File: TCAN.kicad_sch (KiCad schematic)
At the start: 5 parts

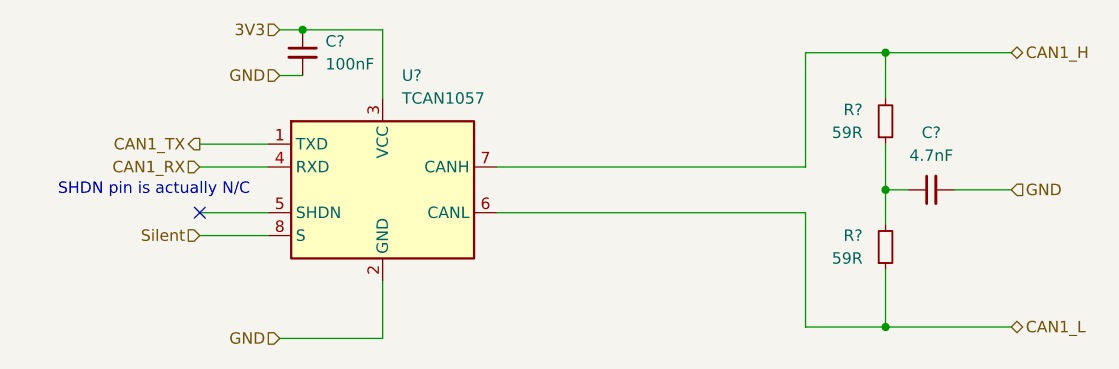
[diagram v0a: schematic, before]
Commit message: Finish routing and add option for using batt mon pads as I2C lines for added GPS
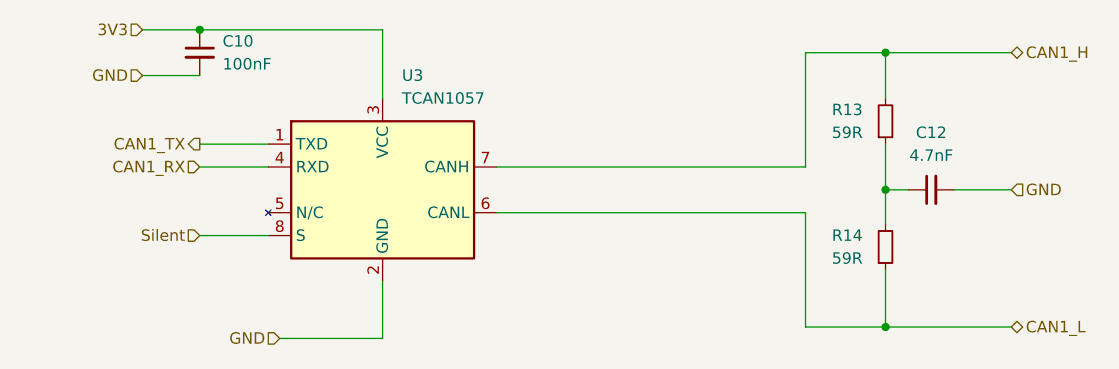
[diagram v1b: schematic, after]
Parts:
- U3: renamed from U?; symbol Interface_CAN_LIN:TCAN330G -> Mad_Symbols:TCAN1057
- gave numbers to parts that had none: 4
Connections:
- net GND: now also U3.9 (GND)
- no-connect marks 1 -> 0
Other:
- note removed: "SHDN pin is actually N/C"
- moved on the sheet: C10
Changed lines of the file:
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@@
 	(generator_version "9.0")
 	(paper "A4")
-	(text "SHDN pin is actually N/C"
-		(exclude_from_sim no)
-		(at 124.46 88.9 0)
-		(effects
-			(font
-				(size 1.27 1.27)
-			)
-		)
-	)
 	(junction
-		(at 140.97 71.12)
+		(at 129.54 71.12)
 		(diameter 0)
 		(color 0 0 0 0)
@@
 		(color 0 0 0 0)
 	)
-	(no_connect
-		(at 129.54 91.44)
-	)
 	(wire
 		(pts
@@
 	(wire
 		(pts
-			(xy 138.43 71.12) (xy 140.97 71.12)
-		)
-		(stroke
-			(width 0)
-			(type default)
-		)
-	)
-	(wire
-		(pts
-			(xy 138.43 76.2) (xy 140.97 76.2)
+			(xy 123.19 71.12) (xy 129.54 71.12)
+		)
+		(stroke
+			(width 0)
+			(type default)
+		)
+	)
+	(wire
+		(pts
+			(xy 123.19 76.2) (xy 129.54 76.2)
 		)
 		(stroke
@@
 	(wire
 		(pts
-			(xy 140.97 71.12) (xy 149.86 71.12)
-		)
-		(stroke
-			(width 0)
-			(type default)
-		)
-	)
-	(wire
-		(pts
 			(xy 129.54 83.82) (xy 137.16 83.82)
 		)
@@
 	(wire
 		(pts
-			(xy 129.54 91.44) (xy 137.16 91.44)
-		)
-		(stroke
-			(width 0)
-			(type default)
-		)
-	)
-	(wire
-		(pts
 			(xy 205.74 73.66) (xy 205.74 78.74)
 		)
@@
 		(pts
 			(xy 196.85 104.14) (xy 196.85 91.44)
+		)
+		(stroke
+			(width 0)
+			(type default)
+		)
+	)
+	(wire
+		(pts
+			(xy 129.54 71.12) (xy 149.86 71.12)
 		)
 		(stroke
@@
 	(hierarchical_label "3V3"
 		(shape input)
-		(at 138.43 71.12 180)
+		(at 123.19 71.12 180)
 		(effects
 			(font
@@
 	(hierarchical_label "GND"
 		(shape input)
-		(at 138.43 76.2 180)
+		(at 123.19 76.2 180)
 		(effects
 			(font
@@
 		(dnp no)
 		(fields_autoplaced yes)
-		(property "Reference" "C?"
+		(property "Reference" "C12"
 			(at 210.8263 82.55 90)
 			(effects
@@
 			(project "L431_RC_Periph"
 				(path "/4cee0169-48cd-4af2-8890-7045155e0b79/6992b08b-1fa8-468e-a7a3-ba5f0cdd154c/59667026-08f2-47e2-8be4-f096db63e523"
-					(reference "C?")
+					(reference "C12")
 					(unit 1)
 				)
@@
 	)
 	(symbol
-		(lib_id "Interface_CAN_LIN:TCAN330G")
+		(lib_id "Mad_Symbols:TCAN1057")
 		(at 149.86 88.9 0)
 		(unit 1)
@@
 		(dnp no)
 		(fields_autoplaced yes)
-		(property "Reference" "U?"
+		(property "Reference" "U3"
 			(at 152.0033 76.2 0)
 			(effects
@@
 		)
 		(pin "7"
+		)
+		(pin "9"
 		)
 		(instances
 			(project "L431_RC_Periph"
 				(path "/4cee0169-48cd-4af2-8890-7045155e0b79/6992b08b-1fa8-468e-a7a3-ba5f0cdd154c/59667026-08f2-47e2-8be4-f096db63e523"
-					(reference "U?")
+					(reference "U3")
 					(unit 1)
 				)
@@
 	(symbol
 		(lib_id "Device:C_Small")
-		(at 140.97 73.66 0)
+		(at 129.54 73.66 0)
 		(mirror y)
 		(unit 1)
@@
 		(dnp no)
 		(fields_autoplaced yes)
-		(property "Reference" "C?"
-			(at 143.51 72.3962 0)
+		(property "Reference" "C10"
+			(at 132.08 72.3962 0)
 			(effects
 				(font
@@
 		)
 		(property "Value" "100nF"
-			(at 143.51 74.9362 0)
+			(at 132.08 74.9362 0)
 			(effects
 				(font
@@
 		)
 		(property "Footprint" "Capacitor_SMD:C_0402_1005Metric"
-			(at 140.97 73.66 0)
+			(at 129.54 73.66 0)
 			(effects
 				(font
@@
 		)
 		(property "Datasheet" "https://www.yageo.com/upload/media/product/productsearch/datasheet/mlcc/UPY-GPHC_X7R_6.3V-to-250V_24.pdf"
-			(at 140.97 73.66 0)
+			(at 129.54 73.66 0)
 			(effects
 				(font
@@
 		)
 		(property "Description" "0.1 µF ±10% 25V Ceramic Capacitor X7R 0402 (1005 Metric)"
-			(at 140.97 73.66 0)
+			(at 129.54 73.66 0)
 			(effects
 				(font
@@
 		)
 		(property "Price" "$0.17"
-			(at 140.97 73.66 0)
+			(at 129.54 73.66 0)
 			(effects
 				(font
@@
 		)
 		(property "Interface" ""
-			(at 140.97 73.66 0)
+			(at 129.54 73.66 0)
 			(effects
 				(font
@@
 		)
 		(property "Rating" "CAP 0402 50V 100 NF X7R"
-			(at 140.97 73.66 0)
+			(at 129.54 73.66 0)
 			(effects
 				(font
@@
 		)
 		(property "Supplier" "Digikey"
-			(at 140.97 73.66 0)
+			(at 129.54 73.66 0)
 			(effects
 				(font
@@
 		)
 		(property "Supplier PN" "13-CC0402KPX7R9BB104CT-ND"
-			(at 140.97 73.66 0)
+			(at 129.54 73.66 0)
 			(effects
 				(font
@@
 		)
 		(property "Manufacturer" "YAGEO"
-			(at 140.97 73.66 0)
+			(at 129.54 73.66 0)
 			(effects
 				(font
@@
 		)
 		(property "MPN" "CC0402KPX7R9BB104"
-			(at 140.97 73.66 0)
+			(at 129.54 73.66 0)
 			(effects
 				(font
@@
 		)
 		(property "Substitute" ""
-			(at 140.97 73.66 0)
+			(at 129.54 73.66 0)
 			(effects
 				(font
@@
 		)
 		(property "LCSC" "C432917"
-			(at 140.97 73.66 0)
+			(at 129.54 73.66 0)
 			(effects
 				(font
@@
 			(project "L431_RC_Periph"
 				(path "/4cee0169-48cd-4af2-8890-7045155e0b79/6992b08b-1fa8-468e-a7a3-ba5f0cdd154c/59667026-08f2-47e2-8be4-f096db63e523"
-					(reference "C?")
+					(reference "C10")
 					(unit 1)
 				)
@@
 		(on_board yes)
 		(dnp no)
-		(property "Reference" "R?"
+		(property "Reference" "R13"
 			(at 203.2 80.0099 0)
 			(effects
@@
 			)
 		)
-		(property "Description" "59 Ohms ±1% 0.063W, 1/16W Chip Resistor 0402 (1005 Metric) Moisture Resistant Thick Film"
+		(property "Description" "Resistor, small symbol"
 			(at 205.74 81.28 0)
 			(effects
@@
 			(project "L431_RC_Periph"
 				(path "/4cee0169-48cd-4af2-8890-7045155e0b79/6992b08b-1fa8-468e-a7a3-ba5f0cdd154c/59667026-08f2-47e2-8be4-f096db63e523"
-					(reference "R?")
+					(reference "R13")
 					(unit 1)
 				)
@@
 		(on_board yes)
 		(dnp no)
-		(property "Reference" "R?"
+		(property "Reference" "R14"
 			(at 203.2 93.9799 0)
 			(effects
@@
 			)
 		)
-		(property "Description" "59 Ohms ±1% 0.063W, 1/16W Chip Resistor 0402 (1005 Metric) Moisture Resistant Thick Film"
+		(property "Description" "Resistor, small symbol"
 			(at 205.74 95.25 0)
 			(effects
@@
 			(project "L431_RC_Periph"
 				(path "/4cee0169-48cd-4af2-8890-7045155e0b79/6992b08b-1fa8-468e-a7a3-ba5f0cdd154c/59667026-08f2-47e2-8be4-f096db63e523"
-					(reference "R?")
+					(reference "R14")
 					(unit 1)
 				)
